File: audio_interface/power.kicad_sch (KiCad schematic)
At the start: 39 parts, among them J3 EXT_5V, U4 LT1172, U5 TPS7A49, U6 TPS7A30

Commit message: Further changes
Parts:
- removed J3: EXT_5V, symbol Connector_Generic:Conn_01x01
- added C30: 0.1u, symbol Device:C
- added C33: 2.2u, symbol Device:C_Polarized_US
- added D1: LED, symbol Device:LED
- added H1, H2, H3, H4: MountingHole_Pad, symbol Mechanical:MountingHole_Pad
- added J3: EXT_5V, symbol Connector:Barrel_Jack
- added J4: EXT_SWITCHED, symbol Connector_Generic:Conn_01x03
- added J5: PROBE_GND, symbol Connector_Generic:Conn_01x04
- added J7: EXT_DIGITAL, symbol Connector_Generic:Conn_01x02
- added J?: D_PWR_SEL, symbol Connector_Generic:Conn_01x03
- added JP16: Jumper_2_Bridged, symbol Jumper:Jumper_2_Bridged
- added R20: 600, symbol Device:R_US
- added U8: L4931, symbol Customs:L4931
- gave numbers to parts that had none: 2
- renumbered C11 to C21, C12 to C22, C13 to C23, C14 to C24, C15 to C25, C16 to C26, C17 to C27, C18 to C28, C19 to C29, C20 to C31, C21 to C32, C22 to C34, C23 to C35, D1 to D2, D2 to D3, JP8 to JP10, JP9 to JP11, JP10 to JP12, JP11 to JP13, JP12 to JP14, JP7 to JP9, R15 to R19, R16 to R21, R17 to R22, R18 to R23, R19 to R24, R20 to R25, R21 to R26, U4 to U5, U5 to U6, U6 to U7
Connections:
- net +12VA: now also J4.1 (Pin_1)
- net +5V: now also R20.1
- net -12VA: now also J4.3 (Pin_3)
- net GNDA: now also J4.2 (Pin_2)
- net GNDD: now also C30.2, C33.2, D1.1 (K), H1.1, H2.1, H3.1, H4.1, J3.2, J5.1 (Pin_1), J5.2 (Pin_2), J5.3 (Pin_3), J5.4 (Pin_4), J7.2 (Pin_2), U8.2 (GND)
- net USB_5V: now also J?.1 (Pin_1)
- net at F1.1, JP10.2 (B): now also J3.1
- new net: C33.1, JP16.1 (A), U8.3 (Output)
- new net: D1.2 (A), R20.2
- new net: C30.1, J?.2 (Pin_2), U8.1 (Input)
- new net +3V3: J7.1 (Pin_1), JP16.2 (B)
- new net +9V: J?.3 (Pin_3)
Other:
- note added: "2A Rating"
- note added: "500mA max (on USB)"
- note added: "700mA max draw"
- note added: "90mA max"
- note added: "Allows for testing USB without bench supply"
- note removed: "350mA max draw"
- note removed: "500mA max"
- moved on the sheet: C28, C29, C31, C32, C34, C35, F1, J6, JP10, JP13, JP14, R23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

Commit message: Added TP and fixed some capacitor values after SPICE sim.
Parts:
- removed C21, C24, C25, C27: 100u, symbol Device:C_Polarized_US
- removed C22: 20n, symbol Device:C
- removed D3: D, symbol Device:D
- removed D4: D_Schottky, symbol Device:D_Schottky
- removed J4: EXT_SWITCHED, symbol Connector_Generic:Conn_01x03
- removed JP12: Jumper_2_Bridged, symbol Jumper:Jumper_2_Bridged
- removed L3: 5u, symbol Device:L
- removed NT1: NetTie_2, symbol Device:NetTie_2
- removed R19: 2k, symbol Device:R_US
- removed R22: 1k5, symbol Device:R_US
- removed U5: LT1172, symbol Customs:LT1172
- added C21: 0.1u, symbol Device:C
- added C22: 4.7u, symbol Device:C_Polarized_US
- added C24: 1u, symbol Device:C
- added C25: 220p, symbol Device:C
- added C?: 10n, symbol Device:C
- added J5: EXT_5VA, symbol Connector_Generic:Conn_01x02
- added J6: EXT_INV, symbol Connector_Generic:Conn_01x02
- added R20: 60k, symbol Device:R_US
- added TP8: 9V, symbol Connector:TestPoint
- added U5: L4931, symbol Customs:L4931
- added U6: LT1931, symbol Customs:LT1931
- C23: value 100u -> 2.2u
- C26: value 100u -> 22u
- J3: value EXT_5V -> EXT_9V
- L1: value 50u -> 15u
- L2: value 5u -> 15u
- R19: renamed from R20; value 600 -> 1k4
- R21: value 13k -> 10k
- R23: renamed from R24; value 105k3 -> 123k
- R25: renamed from R26; value 105k3 -> 123k
- gave numbers to parts that had none: 1
- renumbered C28 to C27, C29 to C28, C30 to C29, C33 to C30, C34 to C33, C35 to C34, J5 to J4, J6 to J7, J7 to J9, JP13 to JP12, JP14 to JP13, JP16 to JP14, R23 to R22, R25 to R24, U6 to U7, U7 to U8, U8 to U9
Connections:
- net +5V is gone; now on net +9V: F1.2, JP9.1 (A), R19.1
- net +9V: now also C33.1, JP10.1 (A), U7.5 (EN), U7.8 (IN), TP8.1
- net GNDA: now also C23.2; no longer C26.2
- net GNDD: now also C26.2, R21.2, C21.2, C22.2, C?.2, J5.2 (Pin_2), J6.2 (Pin_2), U5.2 (GND), U6.2 (GND)
- net USB_5V: no longer JP10.1 (A)
- net at L1.1: now also JP10.2 (B), C22.1, U6.4 (SHDN_n), U6.5 (Vin); no longer JP9.2 (B)
- net at R21.1: now also C25.2, R20.2, U6.3 (NFB); no longer L2.1
- net at C26.1, JP11.1 (A), L2.2: now also C25.1, C?.1, R20.1
- net at F1.1, J3.1: no longer JP10.2 (B)
- net at D2.2 (A): now also L2.1, C24.2; no longer C23.2
- net at L1.2: now also C24.1, U6.1 (SW); no longer C23.1
- removed net +12VA: C33.1, JP11.2 (B), U7.5 (EN), U7.8 (IN)
- net +8V renamed VAA
- net -12VA renamed -9V
- net -9V: now also JP11.2 (B), J6.1 (Pin_1)
- net -8V renamed VSSA
- new net: C21.1, JP9.2 (B), U5.1 (Input)
- new net +5VA: C23.1, J5.1 (Pin_1), U5.3 (Output)
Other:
- note added: "-7V"
- note added: "200mA max"
- note added: "65mA max"
- note added: "7V"
- note removed: "500mA max (on USB)"
- note removed: "700mA max draw"
- note removed: "From Analog Devices Design Note 47"
- moved on the sheet: C29, C30, D1, F1, H1, H2, H3, H4, J3, J4, J8, J9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

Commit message: Added some footprints.
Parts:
- C21, C25: footprint (none) -> Capacitor_SMD:C_0805_2012Metric_Pad1.15x1.40mm_HandSolder
- C24: footprint (none) -> Capacitor_SMD:C_1206_3216Metric_Pad1.42x1.75mm_HandSolder
- C27: renamed from C?; footprint (none) -> Capacitor_SMD:C_0805_2012Metric_Pad1.15x1.40mm_HandSolder
- C28: renamed from C27; footprint (none) -> Capacitor_SMD:C_0805_2012Metric_Pad1.15x1.40mm_HandSolder
- C29: renamed from C28; footprint (none) -> Capacitor_SMD:C_0805_2012Metric_Pad1.15x1.40mm_HandSolder
- C30: renamed from C29; footprint (none) -> Capacitor_SMD:C_0805_2012Metric_Pad1.15x1.40mm_HandSolder
- C32: renamed from C31; footprint (none) -> Capacitor_SMD:C_0805_2012Metric_Pad1.15x1.40mm_HandSolder
- C33: renamed from C32; footprint (none) -> Capacitor_SMD:C_0805_2012Metric_Pad1.15x1.40mm_HandSolder
- JP10, JP11, JP12, JP13, JP14, JP9, R19, R20, R21, R22, R23, R24, R25: footprint (none) -> Resistor_SMD:R_1206_3216Metric_Pad1.42x1.75mm_HandSolder
- TP8: footprint (none) -> TestPoint:TestPoint_Loop_D2.54mm_Drill1.5mm_Beaded
- renumbered C30 to C31, C33 to C34, C34 to C35

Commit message: Finished footprints.
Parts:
- C21, C25, C27, C28, C29, C30, C32, C33: footprint Capacitor_SMD:C_0805_2012Metric_Pad1.15x1.40mm_HandSolder -> Capacitor_SMD:C_0805_2012Metric_Pad1.18x1.45mm_HandSolder
- C22, C23, C26, C31, C34, C35: footprint (none) -> Capacitor_SMD:CP_Elec_6.3x5.2
- C24: footprint Capacitor_SMD:C_1206_3216Metric_Pad1.42x1.75mm_HandSolder -> Capacitor_SMD:C_1206_3216Metric_Pad1.33x1.80mm_HandSolder
- D1: footprint (none) -> LED_SMD:LED_1206_3216Metric_Pad1.42x1.75mm_HandSolder
- D2: footprint (none) -> Diode_SMD:D_1206_3216Metric_Pad1.42x1.75mm_HandSolder
- F1: footprint (none) -> Fuse:Fuse_2920_7451Metric_Pad2.10x5.45mm_HandSolder
- H1, H2, H3, H4: footprint (none) -> MountingHole:MountingHole_3.2mm_M3_Pad
- J3: footprint (none) -> Connector_BarrelJack:BarrelJack_CUI_PJ-063AH_Horizontal
- J4: footprint (none) -> Connector_PinHeader_2.54mm:PinHeader_1x04_P2.54mm_Vertical
- J5, J6, J9: footprint (none) -> Connector_PinHeader_2.54mm:PinHeader_1x02_P2.54mm_Vertical
- J7, J8: footprint (none) -> Connector_PinHeader_2.54mm:PinHeader_1x03_P2.54mm_Vertical
- JP10, JP11, JP12, JP13, JP14, JP9, R19, R20, R21, R22, R23, R24, R25: footprint Resistor_SMD:R_1206_3216Metric_Pad1.42x1.75mm_HandSolder -> Resistor_SMD:R_1206_3216Metric_Pad1.30x1.75mm_HandSolder
- L1, L2: footprint (none) -> Inductor_SMD:L_Taiyo-Yuden_NR-40xx_HandSoldering
- U5, U9: footprint (none) -> Package_TO_SOT_SMD:TO-252-2
- U6: footprint (none) -> Package_TO_SOT_SMD:TSOT-23-5_HandSoldering
- U7, U8: footprint (none) -> Package_SO:VSSOP-8_3.0x3.0mm_P0.65mm

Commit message: Orion's layout
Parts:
- removed C26: 22u, Capacitor_SMD:CP_Elec_6.3x5.2, symbol Device:C_Polarized_US
- added C8: 22u, Capacitor_SMD:CP_Elec_6.3x5.2, symbol Device:C_Polarized_US
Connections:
- net GNDD: now also C8.1
- net at C25.1, C27.1, JP11.1 (A)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: now also C8.2
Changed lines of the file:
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@@
-    (pin "2")
-  )
-  (symbol (lib_id "Device:C_Polarized_US") (at 113.03 173.99 0) (unit 1)
-    (in_bom yes) (on_board yes) (fields_autoplaced)
-    (property "Reference" "C26" (id 0) (at 116.84 172.0849 0)
-      (effects (font (size 1.27 1.27)) (justify left))
-    )
-    (property "Value" "22u" (id 1) (at 116.84 174.6249 0)
-      (effects (font (size 1.27 1.27)) (justify left))
-    )
-    (property "Footprint" "Capacitor_SMD:CP_Elec_6.3x5.2" (id 2) (at 113.03 173.99 0)
-      (effects (font (size 1.27 1.27)) hide)
-    )
-    (property "Datasheet" "~" (id 3) (at 113.03 173.99 0)
-      (effects (font (size 1.27 1.27)) hide)
-    )
-    (pin "1")
     (pin "2")
   )
@@
     (pin "9")
   )
+  (symbol (lib_id "Device:C_Polarized_US") (at 113.03 173.99 180) (unit 1)
+    (in_bom yes) (on_board yes) (fields_autoplaced)
+    (property "Reference" "C8" (id 0) (at 116.84 173.3549 0)
+      (effects (font (size 1.27 1.27)) (justify right))
+    )
+    (property "Value" "22u" (id 1) (at 116.84 175.8949 0)
+      (effects (font (size 1.27 1.27)) (justify right))
+    )
+    (property "Footprint" "Capacitor_SMD:CP_Elec_6.3x5.2" (id 2) (at 113.03 173.99 0)
+      (effects (font (size 1.27 1.27)) hide)
+    )
+    (property "Datasheet" "~" (id 3) (at 113.03 173.99 0)
+      (effects (font (size 1.27 1.27)) hide)
+    )
+    (pin "1")
+    (pin "2")
+  )
   (symbol (lib_id "Mechanical:MountingHole_Pad") (at 92.71 30.48 0) (unit 1)

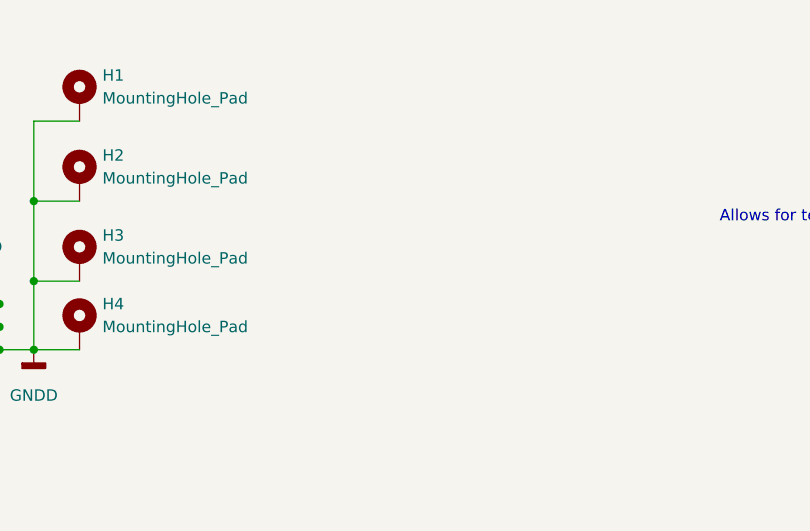
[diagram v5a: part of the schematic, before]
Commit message: Fixed some layout issues. Flipped ADC.
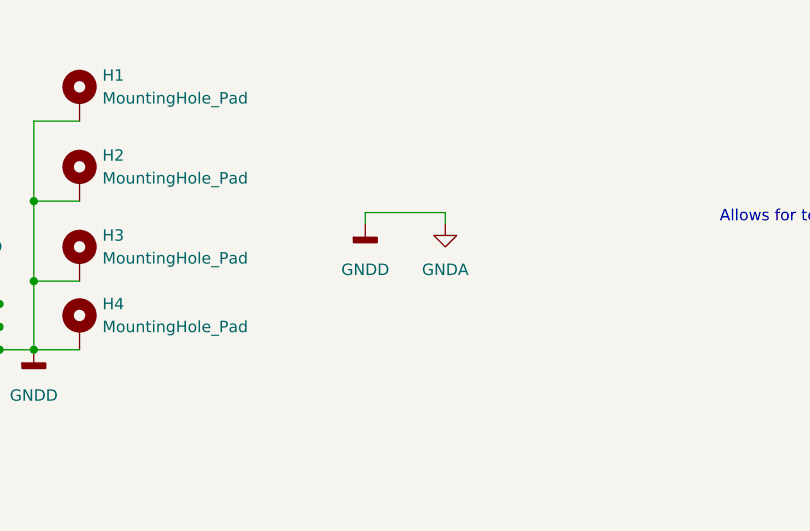
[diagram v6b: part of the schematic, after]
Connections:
- net GNDD is gone; now on net GNDA: C21.2, C22.2, C27.2, C30.2, C31.2, C8.1, D1.1 (K), D2.1 (K), H1.1, H2.1, H3.1, H4.1, J3.2, J4.1 (Pin_1), J4.2 (Pin_2), J4.3 (Pin_3), J4.4 (Pin_4), J5.2 (Pin_2), J6.2 (Pin_2), J9.2 (Pin_2), R21.2, U5.2 (GND), U6.2 (GND), U9.2 (GND)
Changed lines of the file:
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@@
+    (stroke (width 0) (type default) (color 0 0 0 0))
+  )
+  (wire (pts (xy 133.35 34.29) (xy 124.46 34.29))
     (stroke (width 0) (type default) (color 0 0 0 0))
   )
@@
     (stroke (width 0) (type default) (color 0 0 0 0))
   )
+  (wire (pts (xy 133.35 35.56) (xy 133.35 34.29))
+    (stroke (width 0) (type default) (color 0 0 0 0))
+  )
   (wire (pts (xy 137.16 160.02) (xy 137.16 161.29))
     (stroke (width 0) (type default) (color 0 0 0 0))
@@
   )
   (wire (pts (xy 252.73 157.48) (xy 252.73 156.21))
+    (stroke (width 0) (type default) (color 0 0 0 0))
+  )
+  (wire (pts (xy 124.46 34.29) (xy 124.46 35.56))
     (stroke (width 0) (type default) (color 0 0 0 0))
   )
@@
     (pin "5")
   )
+  (symbol (lib_id "power:GNDA") (at 133.35 35.56 0) (unit 1)
+    (in_bom yes) (on_board yes) (fields_autoplaced)
+    (property "Reference" "#PWR0108" (id 0) (at 133.35 41.91 0)
+      (effects (font (size 1.27 1.27)) hide)
+    )
+    (property "Value" "GNDA" (id 1) (at 133.35 40.64 0))
+    (property "Footprint" "" (id 2) (at 133.35 35.56 0)
+      (effects (font (size 1.27 1.27)) hide)
+    )
+    (property "Datasheet" "" (id 3) (at 133.35 35.56 0)
+      (effects (font (size 1.27 1.27)) hide)
+    )
+    (pin "1")
+  )
   (symbol (lib_id "Connector_Generic:Conn_01x03") (at 187.96 26.67 0) (mirror y) (unit 1)
     (in_bom yes) (on_board yes) (fields_autoplaced)
@@
     (pin "9")
   )
+  (symbol (lib_id "power:GNDD") (at 124.46 35.56 0) (unit 1)
+    (in_bom yes) (on_board yes) (fields_autoplaced)
+    (property "Reference" "#PWR0107" (id 0) (at 124.46 41.91 0)
+      (effects (font (size 1.27 1.27)) hide)
+    )
+    (property "Value" "GNDD" (id 1) (at 124.46 40.64 0))
+    (property "Footprint" "" (id 2) (at 124.46 35.56 0)
+      (effects (font (size 1.27 1.27)) hide)
+    )
+    (property "Datasheet" "" (id 3) (at 124.46 35.56 0)
+      (effects (font (size 1.27 1.27)) hide)
+    )
+    (pin "1")
+  )
   (symbol (lib_id "power:+9V") (at 27.94 143.51 0) (unit 1)

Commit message: Changed some footprints and grounding.
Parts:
- C22, C23, C31: footprint Capacitor_SMD:CP_Elec_6.3x5.2 -> Capacitor_SMD:CP_Elec_4x5.4
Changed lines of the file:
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@@
       (effects (font (size 1.27 1.27)) (justify left))
     )
-    (property "Footprint" "Capacitor_SMD:CP_Elec_6.3x5.2" (id 2) (at 82.55 91.44 0)
+    (property "Footprint" "Capacitor_SMD:CP_Elec_4x5.4" (id 2) (at 82.55 91.44 0)
       (effects (font (size 1.27 1.27)) hide)
     )
@@
       (effects (font (size 1.27 1.27)) (justify left))
     )
-    (property "Footprint" "Capacitor_SMD:CP_Elec_6.3x5.2" (id 2) (at 247.65 31.75 0)
+    (property "Footprint" "Capacitor_SMD:CP_Elec_4x5.4" (id 2) (at 247.65 31.75 0)
       (effects (font (size 1.27 1.27)) hide)
     )
@@
       (effects (font (size 1.27 1.27)) (justify left))
     )
-    (property "Footprint" "Capacitor_SMD:CP_Elec_6.3x5.2" (id 2) (at 48.26 167.64 0)
-      (effects (font (size 1.27 1.27)) hide)
-    )
+    (property "Footprint" "Capacitor_SMD:CP_Elec_4x5.4" (id 2) (at 48.26 167.64 0)
+      (effects (font (size 1.27 1.27)) hide)
+    )

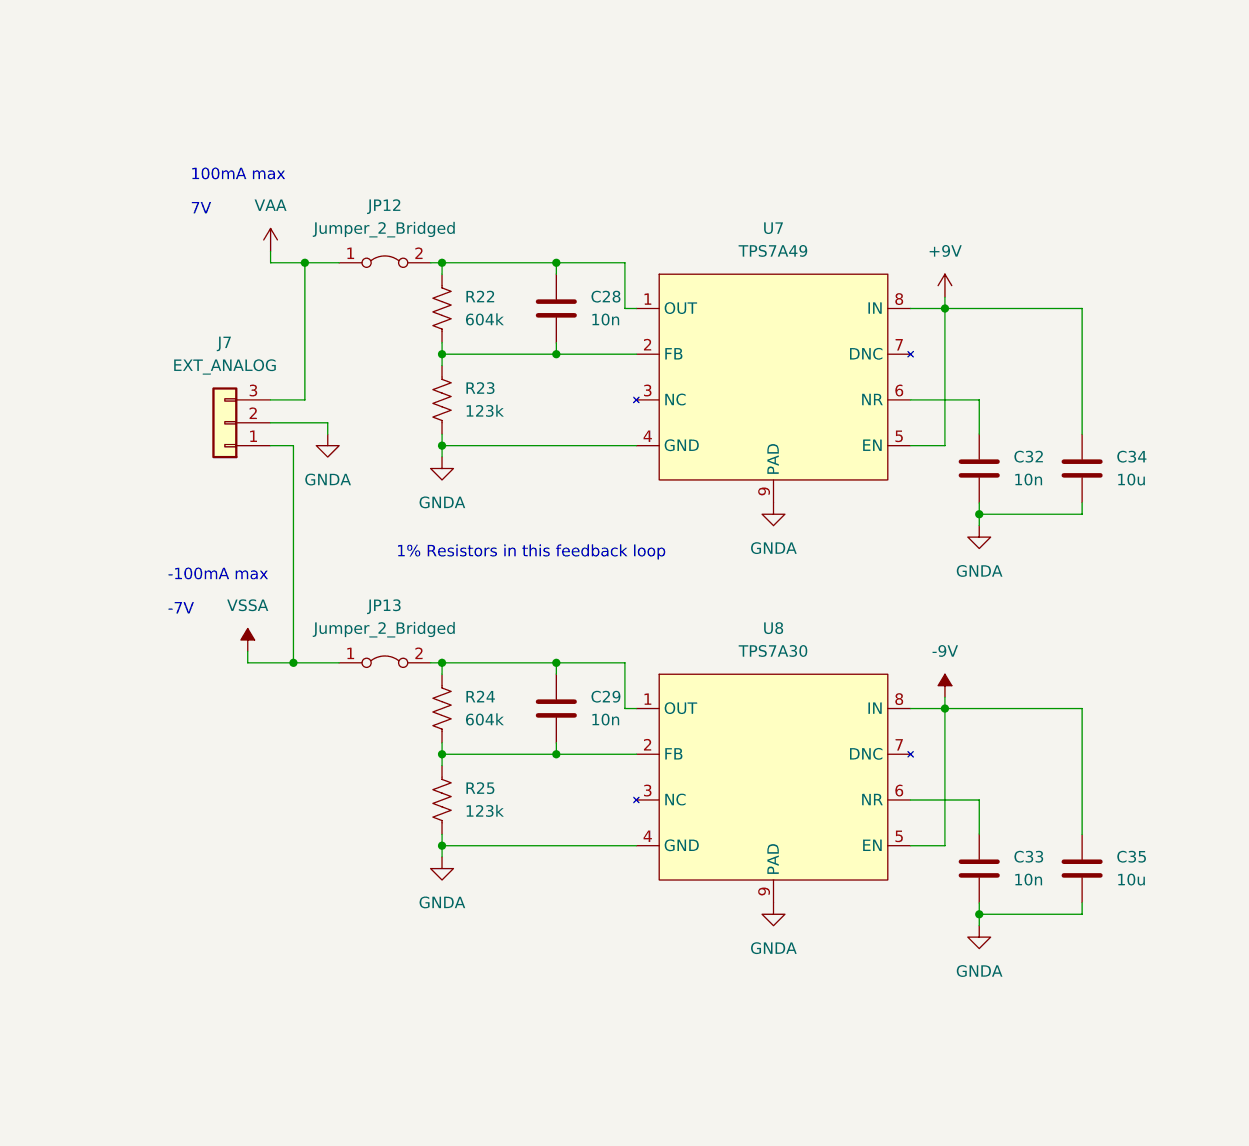
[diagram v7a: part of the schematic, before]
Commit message: Changed pin mappings for easier layout. Redid layout for better ground plane.
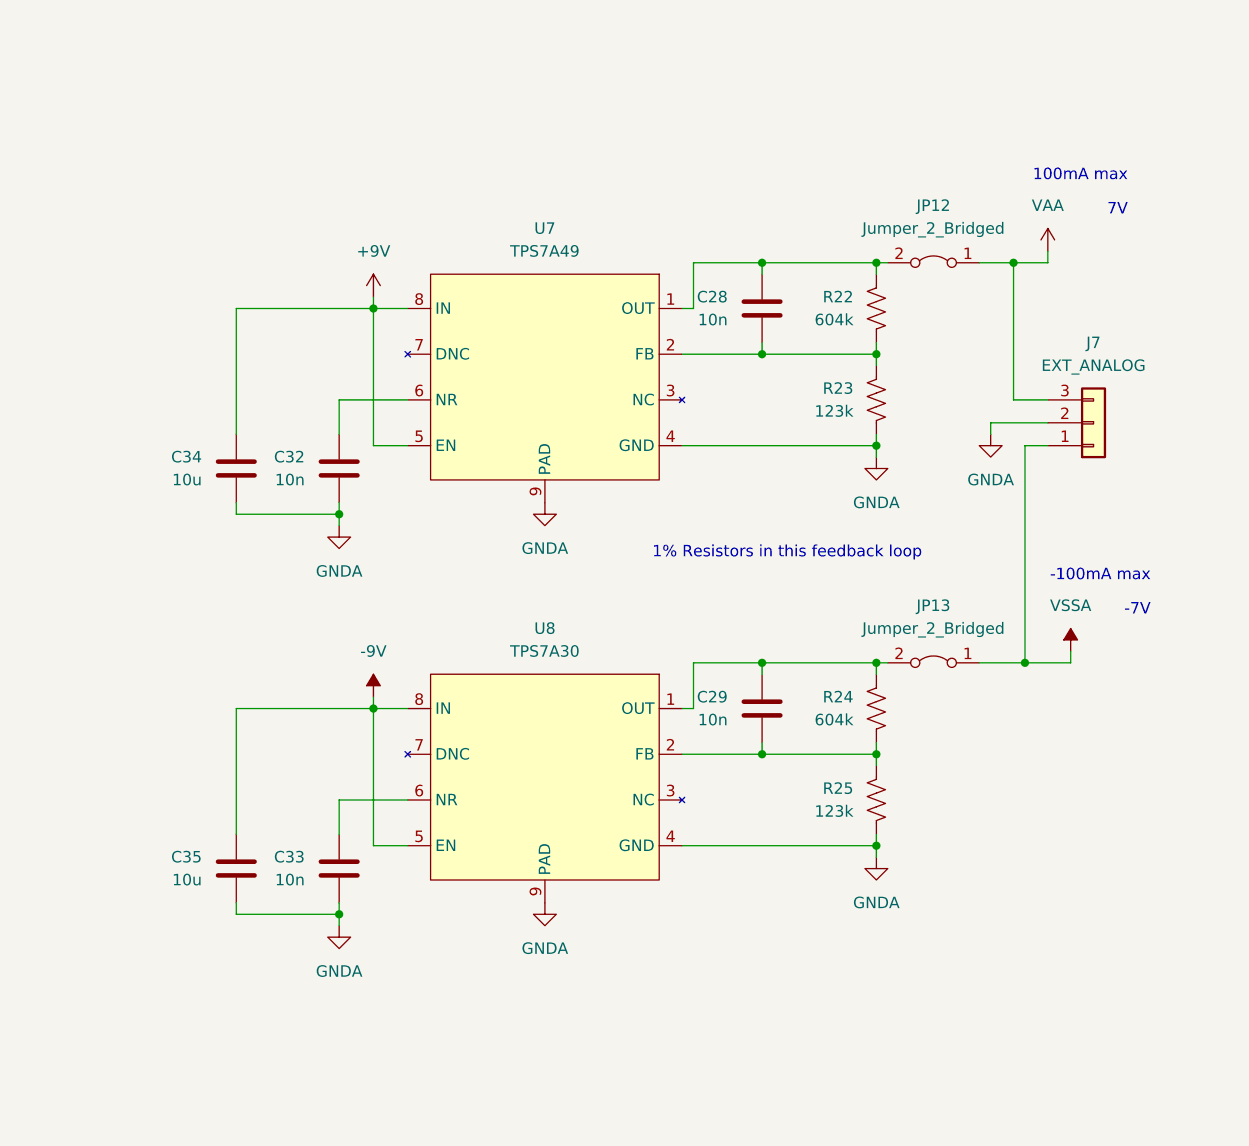
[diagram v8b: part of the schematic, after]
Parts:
- C22, C23, C31: footprint Capacitor_SMD:CP_Elec_4x5.4 -> Capacitor_SMD:C_1206_3216Metric_Pad1.33x1.80mm_HandSolder
- C34, C35: footprint Capacitor_SMD:CP_Elec_6.3x5.2 -> Capacitor_SMD:C_1206_3216Metric_Pad1.33x1.80mm_HandSolder
- C8: footprint Capacitor_SMD:CP_Elec_6.3x5.2 -> Capacitor_SMD:CP_Elec_4x5.4
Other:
- moved on the sheet: C28, C29, C32, C33, C34, C35, J7, JP12, JP13, R22, R23, R24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
